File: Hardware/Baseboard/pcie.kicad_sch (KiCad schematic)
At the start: 20 parts, among them J4 MDT275M02001

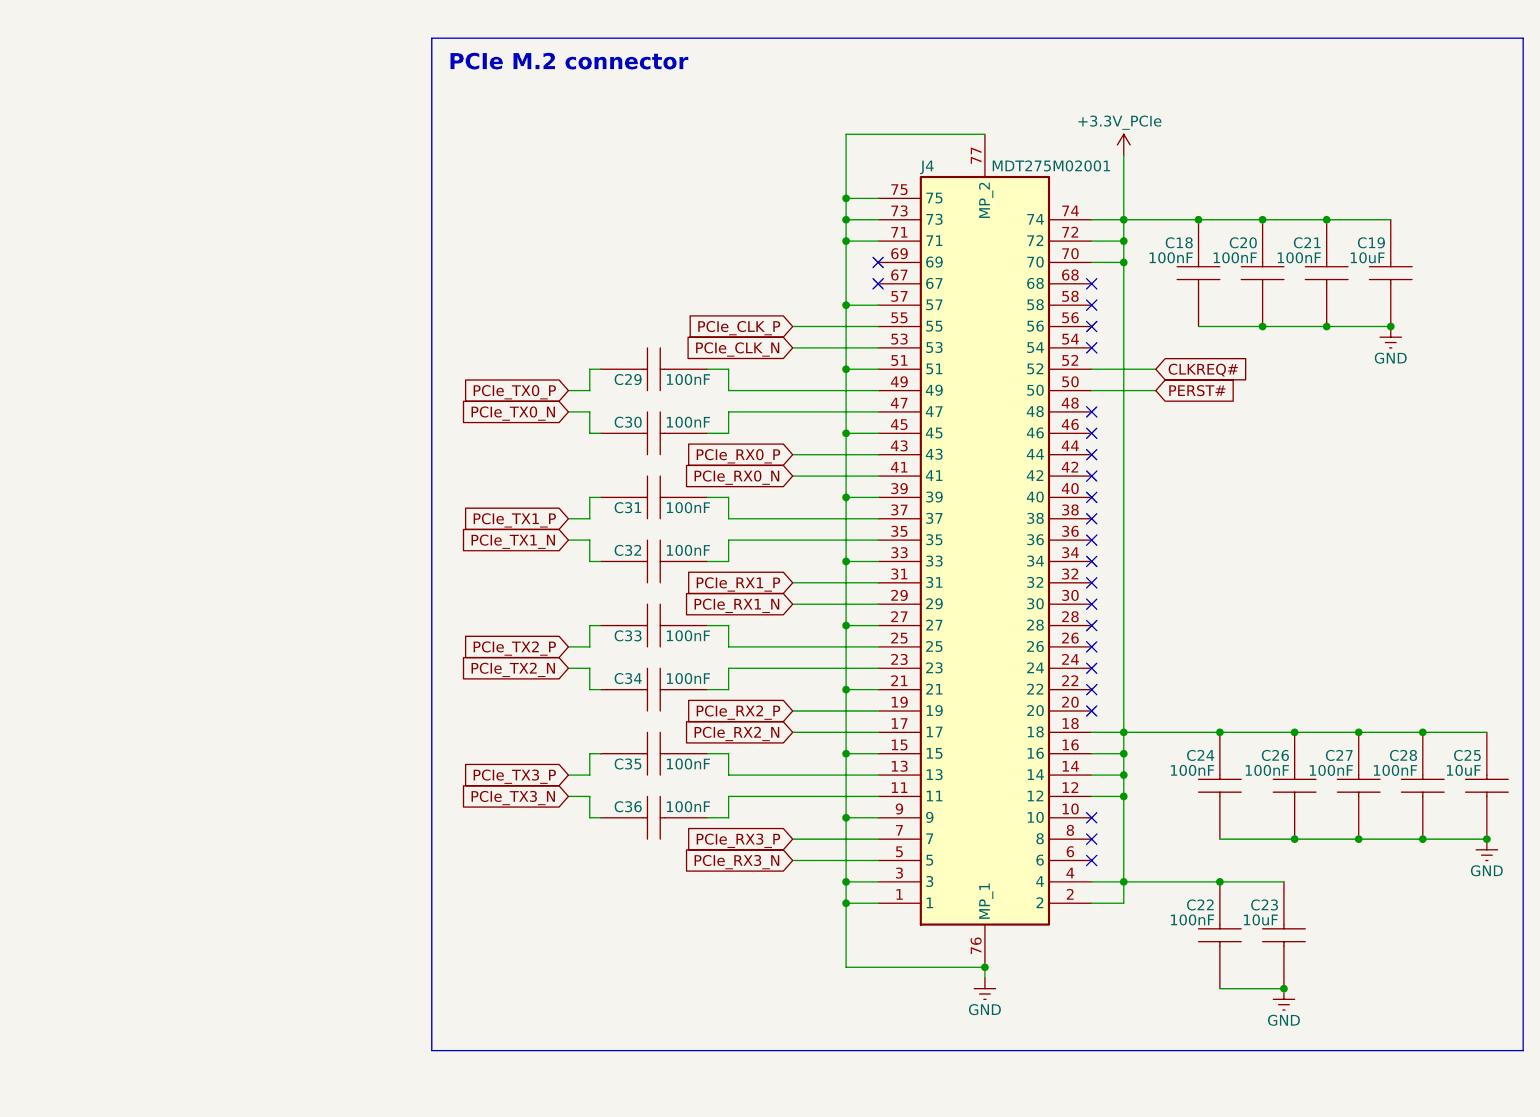
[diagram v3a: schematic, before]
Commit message: PCIe M.2 pull-ups
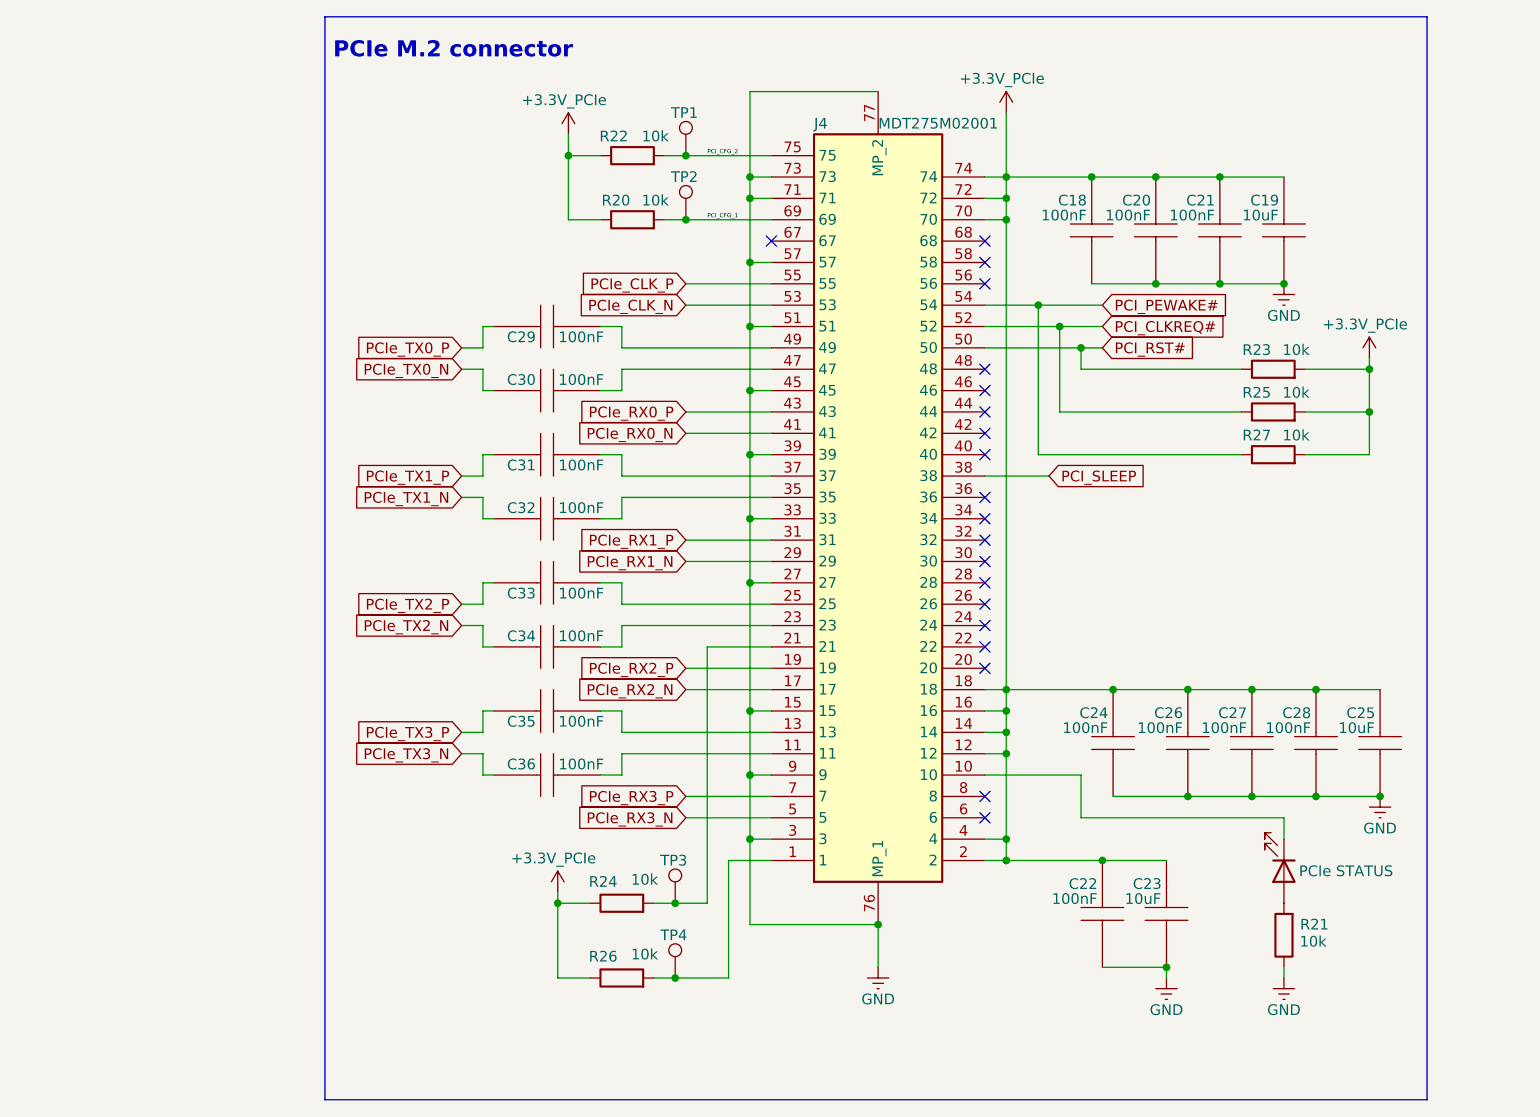
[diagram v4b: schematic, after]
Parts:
- added D1: PCIe STATUS, LED_SMD:LED_0805_2012Metric, symbol Device:LED
- added R20, R21, R22, R23, R24, R25, R26, R27: 10k, Resistor_SMD:R_0402_1005Metric, symbol Device:R
- added TP1, TP2, TP3, TP4: PCI_CFG_2, symbol Connector:TestPoint
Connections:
- net +3.3V_PCIe: now also R20.1, R22.1, R23.2, R24.1, R25.2, R26.1, R27.2
- net GND: now also R21.1; no longer J4.1, J4.21, J4.75
- net at J4.10: now also D1.1 (K)
- net PCI_SLEEP: now reaches J4.38
- net PCI_PEWAKE#: now reaches J4.54
- net PCI_PEWAKE#: now also R27.1
- net PCI_CFG_1: now reaches J4.69
- net PCI_CFG_1: now also R20.2, TP2.1
- net CLKREQ# renamed PCI_CLKREQ#
- net PCI_CLKREQ#: now also R25.1
- net PERST# renamed PCI_RST#
- net PCI_RST#: now also R23.1
- new net: J4.21, R24.2, TP3.1
- new net: J4.1, R26.2, TP4.1
- new net: D1.2 (A), R21.2
- new net PCI_CFG_2: J4.75, R22.2, TP1.1
- no-connect marks 24 -> 20
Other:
- moved on the sheet: C18, C19, C20, C21, C22, C23, C24, C25, C26, C27, C28, C29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

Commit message: SOM: power supplies
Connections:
- net PCI_CFG_0: now reaches J4.21, R24.2, TP3.1
- net PCI_CFG_3: now reaches J4.1, R26.2, TP4.1
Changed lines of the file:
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@@
+		)
+	)
+	(label "PCI_CFG_0"
+		(at 128.27 101.6 0)
+		(effects
+			(font
+				(size 0.508 0.508)
+			)
+			(justify left bottom)
+		)
+	)
+	(label "PCI_CFG_3"
+		(at 131.826 127 0)
+		(effects
+			(font
+				(size 0.508 0.508)
+			)
+			(justify left bottom)
 		)
 	)
